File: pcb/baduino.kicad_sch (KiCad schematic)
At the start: 24 parts, among them J1 USB_A, J3 TF-015, SW1 SW_DIP_x04, U1 ATmega32U4-M, U2 MIC5219-3.3YM5, X1 ASE-xxxMHz

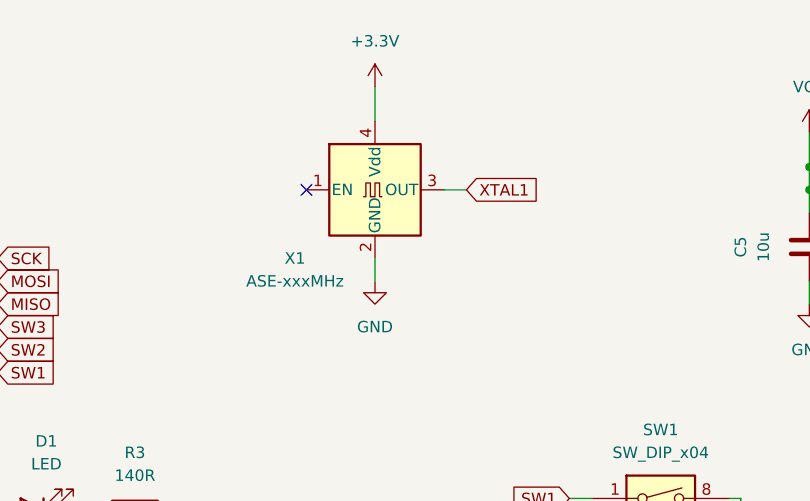
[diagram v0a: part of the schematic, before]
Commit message: switch to non powered crystal oscillator
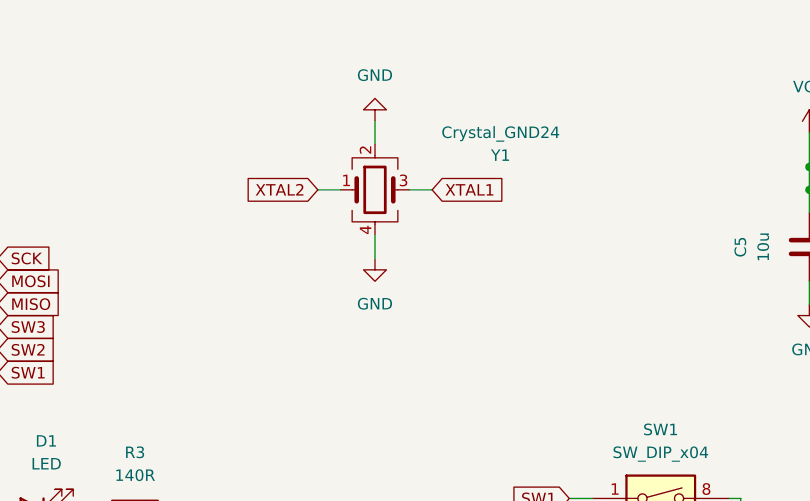
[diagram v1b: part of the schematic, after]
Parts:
- removed X1: ASE-xxxMHz, Crystal:Crystal_SMD_3225-4Pin_3.2x2.5mm_HandSoldering, symbol Oscillator:ASE-xxxMHz
- added Y1: Crystal_GND24, Crystal:Crystal_SMD_3225-4Pin_3.2x2.5mm_HandSoldering, symbol Device:Crystal_GND24
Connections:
- net GND: now also Y1.2, Y1.4
- net XTAL1: now also Y1.3
- net XTAL2: now also Y1.1
- no-connect marks 27 -> 26
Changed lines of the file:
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@@
   (no_connect (at 100.33 78.74))
   (no_connect (at 100.33 104.14))
-  (no_connect (at 138.43 35.56))
   (no_connect (at 154.94 114.3))
   (no_connect (at 100.33 40.64))
@@
     (stroke (width 0) (type default))
   )
+  (wire (pts (xy 146.05 27.94) (xy 146.05 30.48))
+    (stroke (width 0) (type default))
+  )
   (wire (pts (xy 100.33 81.28) (xy 104.14 81.28))
     (stroke (width 0) (type default))
@@
     (stroke (width 0) (type default))
   )
-  (wire (pts (xy 153.67 35.56) (xy 156.21 35.56))
+  (wire (pts (xy 149.86 35.56) (xy 152.4 35.56))
     (stroke (width 0) (type default))
   )
@@
     (stroke (width 0) (type default))
   )
-  (wire (pts (xy 146.05 24.13) (xy 146.05 27.94))
-    (stroke (width 0) (type default))
-  )
   (wire (pts (xy 82.55 125.73) (xy 85.09 125.73))
     (stroke (width 0) (type default))
@@
     (stroke (width 0) (type default))
   )
-  (wire (pts (xy 146.05 45.72) (xy 146.05 43.18))
+  (wire (pts (xy 146.05 43.18) (xy 146.05 40.64))
     (stroke (width 0) (type default))
   )
@@
   )
   (wire (pts (xy 66.04 60.96) (xy 67.31 60.96))
+    (stroke (width 0) (type default))
+  )
+  (wire (pts (xy 142.24 35.56) (xy 139.7 35.56))
     (stroke (width 0) (type default))
   )
@@
     )
   )
-  (global_label "XTAL1" (shape input) (at 156.21 35.56 0) (fields_autoplaced)
-    (effects (font (size 1.27 1.27)) (justify left))
-    (property "Intersheetrefs" "${INTERSHEET_REFS}" (at 164.6985 35.56 0)
-      (effects (font (size 1.27 1.27)) (justify left) hide)
-    )
-  )
   (global_label "SW3" (shape input) (at 104.14 50.8 0) (fields_autoplaced)
     (effects (font (size 1.27 1.27)) (justify left))
@@
     )
   )
+  (global_label "XTAL1" (shape input) (at 152.4 35.56 0) (fields_autoplaced)
+    (effects (font (size 1.27 1.27)) (justify left))
+    (property "Intersheetrefs" "${INTERSHEET_REFS}" (at 160.8885 35.56 0)
+      (effects (font (size 1.27 1.27)) (justify left) hide)
+    )
+  )
   (global_label "RST" (shape input) (at 66.04 40.64 180) (fields_autoplaced)
     (effects (font (size 1.27 1.27)) (justify right))
@@
     )
   )
+  (global_label "XTAL2" (shape input) (at 139.7 35.56 180) (fields_autoplaced)
+    (effects (font (size 1.27 1.27)) (justify right))
+    (property "Intersheetrefs" "${INTERSHEET_REFS}" (at 131.2115 35.56 0)
+      (effects (font (size 1.27 1.27)) (justify right) hide)
+    )
+  )
   (global_label "SCK" (shape input) (at 104.14 43.18 0) (fields_autoplaced)
     (effects (font (size 1.27 1.27)) (justify left))
@@
     )
   )
+  (symbol (lib_id "Device:Crystal_GND24") (at 146.05 35.56 0) (unit 1)
+    (in_bom yes) (on_board yes) (dnp no)
+    (property "Reference" "Y1" (at 160.02 31.75 0)
+      (effects (font (size 1.27 1.27)))
+    )
+    (property "Value" "Crystal_GND24" (at 160.02 29.21 0)
+      (effects (font (size 1.27 1.27)))
+    )
+    (property "Footprint" "Crystal:Crystal_SMD_3225-4Pin_3.2x2.5mm_HandSoldering" (at 146.05 35.56 0)
+      (effects (font (size 1.27 1.27)) hide)
+    )
+    (property "Datasheet" "~" (at 146.05 35.56 0)
+      (effects (font (size 1.27 1.27)) hide)
+    )
+    (pin "1")
+    (pin "2")
+    (pin "3")
+    (pin "4")
+    (instances
+      (project "baduino"
+        (path "/2ecfceef-69cc-4d5d-8c2d-e9f0f72cc907"
+          (reference "Y1") (unit 1)
+        )
+      )
+    )
+  )
   (symbol (lib_id "Connector:TestPoint") (at 90.17 160.02 270) (unit 1)
     (in_bom yes) (on_board yes) (dnp no)
@@
     )
   )
-  (symbol (lib_id "power:GND") (at 146.05 45.72 0) (unit 1)
-    (in_bom yes) (on_board yes) (dnp no) (fields_autoplaced)
-    (property "Reference" "#PWR021" (at 146.05 52.07 0)
-      (effects (font (size 1.27 1.27)) hide)
-    )
-    (property "Value" "GND" (at 146.05 50.8 0)
-      (effects (font (size 1.27 1.27)))
-    )
-    (property "Footprint" "" (at 146.05 45.72 0)
-      (effects (font (size 1.27 1.27)) hide)
-    )
-    (property "Datasheet" "" (at 146.05 45.72 0)
+  (symbol (lib_id "power:GND") (at 146.05 43.18 0) (unit 1)
+    (in_bom yes) (on_board yes) (dnp no) (fields_autoplaced)
+    (property "Reference" "#PWR021" (at 146.05 49.53 0)
+      (effects (font (size 1.27 1.27)) hide)
+    )
+    (property "Value" "GND" (at 146.05 48.26 0)
+      (effects (font (size 1.27 1.27)))
+    )
+    (property "Footprint" "" (at 146.05 43.18 0)
+      (effects (font (size 1.27 1.27)) hide)
+    )
+    (property "Datasheet" "" (at 146.05 43.18 0)
       (effects (font (size 1.27 1.27)) hide)
     )
@@
         (path "/2ecfceef-69cc-4d5d-8c2d-e9f0f72cc907"
           (reference "C4") (unit 1)
-        )
-      )
-    )
-  )
-  (symbol (lib_id "power:+3.3V") (at 146.05 24.13 0) (unit 1)
-    (in_bom yes) (on_board yes) (dnp no) (fields_autoplaced)
-    (property "Reference" "#PWR022" (at 146.05 27.94 0)
-      (effects (font (size 1.27 1.27)) hide)
-    )
-    (property "Value" "+3.3V" (at 146.05 19.05 0)
-      (effects (font (size 1.27 1.27)))
-    )
-    (property "Footprint" "" (at 146.05 24.13 0)
-      (effects (font (size 1.27 1.27)) hide)
-    )
-    (property "Datasheet" "" (at 146.05 24.13 0)
-      (effects (font (size 1.27 1.27)) hide)
-    )
-    (pin "1")
-    (instances
-      (project "baduino"
-        (path "/2ecfceef-69cc-4d5d-8c2d-e9f0f72cc907"
-          (reference "#PWR022") (unit 1)
         )
       )
@@
     )
   )
-  (symbol (lib_id "Oscillator:ASE-xxxMHz") (at 146.05 35.56 0) (unit 1)
-    (in_bom yes) (on_board yes) (dnp no)
-    (property "Reference" "X1" (at 137.16 43.18 0)
-      (effects (font (size 1.27 1.27)))
-    )
-    (property "Value" "ASE-xxxMHz" (at 137.16 45.72 0)
-      (effects (font (size 1.27 1.27)))
-    )
-    (property "Footprint" "Crystal:Crystal_SMD_3225-4Pin_3.2x2.5mm_HandSoldering" (at 163.83 44.45 0)
-      (effects (font (size 1.27 1.27)) hide)
-    )
-    (property "Datasheet" "http://www.abracon.com/Oscillators/ASV.pdf" (at 143.51 35.56 0)
-      (effects (font (size 1.27 1.27)) hide)
-    )
-    (pin "1")
-    (pin "2")
-    (pin "3")
-    (pin "4")
-    (instances
-      (project "baduino"
-        (path "/2ecfceef-69cc-4d5d-8c2d-e9f0f72cc907"
-          (reference "X1") (unit 1)
-        )
-      )
-    )
-  )
   (symbol (lib_id "power:GND") (at 82.55 128.27 0) (unit 1)
     (in_bom yes) (on_board yes) (dnp no) (fields_autoplaced)
@@
         )
       )
+    )
+  )
+  (symbol (lib_id "power:GND") (at 146.05 27.94 180) (unit 1)
+    (in_bom yes) (on_board yes) (dnp no) (fields_autoplaced)
+    (property "Reference" "#PWR022" (at 146.05 21.59 0)
+      (effects (font (size 1.27 1.27)) hide)
+    )
+    (property "Value" "GND" (at 146.05 22.86 0)
+      (effects (font (size 1.27 1.27)))
+    )
+    (property "Footprint" "" (at 146.05 27.94 0)
+      (effects (font (size 1.27 1.27)) hide)
+    )
+    (property "Datasheet" "" (at 146.05 27.94 0)
+      (effects (font (size 1.27 1.27)) hide)
+    )
+    (pin "1")
+    (instances
+      (project "baduino"
+        (path "/2ecfceef-69cc-4d5d-8c2d-e9f0f72cc907"
+          (reference "#PWR022") (unit 1)
+        )
+      )
